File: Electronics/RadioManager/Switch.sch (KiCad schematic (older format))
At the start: 17 parts, among them U1 KSZ8995FQI

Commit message: Annotate existing components
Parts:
- gave numbers to parts that had none: 16
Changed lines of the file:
@@
 Connection ~ 5000 3300
 $Comp
-L +1.8V #PWR?
+L +1.8V #PWR9
 U 1 1 5410F4E8
 P 6200 1700
-F 0 "#PWR?" H 6200 1840 20  0001 C CNN
+F 0 "#PWR9" H 6200 1840 20  0001 C CNN
 F 1 "+1.8V" H 6200 1810 30  0000 C CNN
 F 2 "" H 6200 1700 60  0000 C CNN
@@
 VDDAP
 $Comp
-L C C?
+L C C1
 U 1 1 5410F4F7
 P 6200 2150
-F 0 "C?" H 6250 2300 60  0000 L CNN
+F 0 "C1" H 6250 2300 60  0000 L CNN
 F 1 "C" H 6250 2000 60  0000 L CNN
 F 2 "~" H 6200 2150 60  0000 C CNN
@@
 Connection ~ 6200 1800
 $Comp
-L GND #PWR?
+L GND #PWR10
 U 1 1 5410F557
 P 6200 2500
-F 0 "#PWR?" H 6200 2500 30  0001 C CNN
+F 0 "#PWR10" H 6200 2500 30  0001 C CNN
 F 1 "GND" H 6200 2430 30  0001 C CNN
 F 2 "" H 6200 2500 60  0000 C CNN
@@
 	6200 2500 6200 2400
 $Comp
-L +1.8V #PWR?
+L +1.8V #PWR11
 U 1 1 5410F589
 P 6200 2800
-F 0 "#PWR?" H 6200 2940 20  0001 C CNN
+F 0 "#PWR11" H 6200 2940 20  0001 C CNN
 F 1 "+1.8V" H 6200 2910 30  0000 C CNN
 F 2 "" H 6200 2800 60  0000 C CNN
@@
 VDDAR
 $Comp
-L C C?
+L C C2
 U 1 1 5410F592
 P 6200 3250
-F 0 "C?" H 6250 3400 60  0000 L CNN
+F 0 "C2" H 6250 3400 60  0000 L CNN
 F 1 "C" H 6250 3100 60  0000 L CNN
 F 2 "~" H 6200 3250 60  0000 C CNN
@@
 Connection ~ 6200 2900
 $Comp
-L GND #PWR?
+L GND #PWR12
 U 1 1 5410F59B
 P 6200 3600
-F 0 "#PWR?" H 6200 3600 30  0001 C CNN
+F 0 "#PWR12" H 6200 3600 30  0001 C CNN
 F 1 "GND" H 6200 3530 30  0001 C CNN
 F 2 "" H 6200 3600 60  0000 C CNN
@@
 	6200 3600 6200 3500
 $Comp
-L +3.3V #PWR?
+L +3.3V #PWR24
 U 1 1 5410F5A5
 P 7400 3900
-F 0 "#PWR?" H 7400 3860 30  0001 C CNN
+F 0 "#PWR24" H 7400 3860 30  0001 C CNN
 F 1 "+3.3V" H 7400 4010 30  0000 C CNN
 F 2 "" H 7400 3900 60  0000 C CNN
@@
 VDDAT
 $Comp
-L C C?
+L C C12
 U 1 1 5410F5B4
 P 7400 4350
-F 0 "C?" H 7450 4500 60  0000 L CNN
+F 0 "C12" H 7450 4500 60  0000 L CNN
 F 1 "C" H 7450 4200 60  0000 L CNN
 F 2 "~" H 7400 4350 60  0000 C CNN
@@
 $EndComp
 $Comp
-L GND #PWR?
+L GND #PWR25
 U 1 1 5410F5BA
 P 7400 4700
-F 0 "#PWR?" H 7400 4700 30  0001 C CNN
+F 0 "#PWR25" H 7400 4700 30  0001 C CNN
 F 1 "GND" H 7400 4630 30  0001 C CNN
 F 2 "" H 7400 4700 60  0000 C CNN
@@
 Connection ~ 7400 4000
 $Comp
-L +1.8V #PWR?
+L +1.8V #PWR15
 U 1 1 5410F641
 P 6600 1700
-F 0 "#PWR?" H 6600 1840 20  0001 C CNN
+F 0 "#PWR15" H 6600 1840 20  0001 C CNN
 F 1 "+1.8V" H 6600 1810 30  0000 C CNN
 F 2 "" H 6600 1700 60  0000 C CNN
@@
 VDDC
 $Comp
-L C C?
+L C C4
 U 1 1 5410F64A
 P 6600 2150
-F 0 "C?" H 6650 2300 60  0000 L CNN
+F 0 "C4" H 6650 2300 60  0000 L CNN
 F 1 "C" H 6650 2000 60  0000 L CNN
 F 2 "~" H 6600 2150 60  0000 C CNN
@@
 Connection ~ 6600 1800
 $Comp
-L GND #PWR?
+L GND #PWR16
 U 1 1 5410F653
 P 6600 2500
-F 0 "#PWR?" H 6600 2500 30  0001 C CNN
+F 0 "#PWR16" H 6600 2500 30  0001 C CNN
 F 1 "GND" H 6600 2430 30  0001 C CNN
 F 2 "" H 6600 2500 60  0000 C CNN
@@
 	6600 2500 6600 2400
 $Comp
-L +3.3V #PWR?
+L +3.3V #PWR13
 U 1 1 5410F65B
 P 6200 3900
-F 0 "#PWR?" H 6200 3860 30  0001 C CNN
+F 0 "#PWR13" H 6200 3860 30  0001 C CNN
 F 1 "+3.3V" H 6200 4010 30  0000 C CNN
 F 2 "" H 6200 3900 60  0000 C CNN
@@
 VDDIO
 $Comp
-L C C?
+L C C3
 U 1 1 5410F664
 P 6200 4350
-F 0 "C?" H 6250 4500 60  0000 L CNN
+F 0 "C3" H 6250 4500 60  0000 L CNN
 F 1 "C" H 6250 4200 60  0000 L CNN
 F 2 "~" H 6200 4350 60  0000 C CNN
@@
 $EndComp
 $Comp
-L GND #PWR?
+L GND #PWR14
 U 1 1 5410F66A
 P 6200 4700
-F 0 "#PWR?" H 6200 4700 30  0001 C CNN
+F 0 "#PWR14" H 6200 4700 30  0001 C CNN
 F 1 "GND" H 6200 4630 30  0001 C CNN
 F 2 "" H 6200 4700 60  0000 C CNN
@@
 Connection ~ 6200 4000
 $Comp
-L C C?
+L C C7
 U 1 1 5410F677
 P 7000 2150
-F 0 "C?" H 7050 2300 60  0000 L CNN
+F 0 "C7" H 7050 2300 60  0000 L CNN
 F 1 "C" H 7050 2000 60  0000 L CNN
 F 2 "~" H 7000 2150 60  0000 C CNN
@@
 $EndComp
 $Comp
-L C C?
+L C C10
 U 1 1 5410F67F
 P 7400 2150
-F 0 "C?" H 7450 2300 60  0000 L CNN
+F 0 "C10" H 7450 2300 60  0000 L CNN
 F 1 "C" H 7450 2000 60  0000 L CNN
 F 2 "~" H 7400 2150 60  0000 C CNN
@@
 Connection ~ 7000 1800
 $Comp
-L GND #PWR?
+L GND #PWR19
 U 1 1 5410F6F2
 P 7000 2500
-F 0 "#PWR?" H 7000 2500 30  0001 C CNN
+F 0 "#PWR19" H 7000 2500 30  0001 C CNN
 F 1 "GND" H 7000 2430 30  0001 C CNN
 F 2 "" H 7000 2500 60  0000 C CNN
@@
 $EndComp
 $Comp
-L GND #PWR?
+L GND #PWR22
 U 1 1 5410F6F8
 P 7400 2500
-F 0 "#PWR?" H 7400 2500 30  0001 C CNN
+F 0 "#PWR22" H 7400 2500 30  0001 C CNN
 F 1 "GND" H 7400 2430 30  0001 C CNN
 F 2 "" H 7400 2500 60  0000 C CNN
@@
 	7000 2400 7000 2500
 $Comp
-L C C?
+L C C5
 U 1 1 5410F773
 P 6600 3250
-F 0 "C?" H 6650 3400 60  0000 L CNN
+F 0 "C5" H 6650 3400 60  0000 L CNN
 F 1 "C" H 6650 3100 60  0000 L CNN
 F 2 "~" H 6600 3250 60  0000 C CNN
@@
 $EndComp
 $Comp
-L C C?
+L C C8
 U 1 1 5410F77B
 P 7000 3250
-F 0 "C?" H 7050 3400 60  0000 L CNN
+F 0 "C8" H 7050 3400 60  0000 L CNN
 F 1 "C" H 7050 3100 60  0000 L CNN
 F 2 "~" H 7000 3250 60  0000 C CNN
@@
 $EndComp
 $Comp
-L C C?
+L C C11
 U 1 1 5410F783
 P 7400 3250
-F 0 "C?" H 7450 3400 60  0000 L CNN
+F 0 "C11" H 7450 3400 60  0000 L CNN
 F 1 "C" H 7450 3100 60  0000 L CNN
 F 2 "~" H 7400 3250 60  0000 C CNN
@@
 $EndComp
 $Comp
-L C C?
+L C C13
 U 1 1 5410F78B
 P 7800 3250
-F 0 "C?" H 7850 3400 60  0000 L CNN
+F 0 "C13" H 7850 3400 60  0000 L CNN
 F 1 "C" H 7850 3100 60  0000 L CNN
 F 2 "~" H 7800 3250 60  0000 C CNN
@@
 $EndComp
 $Comp
-L C C?
+L C C15
 U 1 1 5410F793
 P 8200 3250
-F 0 "C?" H 8250 3400 60  0000 L CNN
+F 0 "C15" H 8250 3400 60  0000 L CNN
 F 1 "C" H 8250 3100 60  0000 L CNN
 F 2 "~" H 8200 3250 60  0000 C CNN
@@
 Connection ~ 6600 2900
 $Comp
-L GND #PWR?
+L GND #PWR17
 U 1 1 5410F90F
 P 6600 3600
-F 0 "#PWR?" H 6600 3600 30  0001 C CNN
+F 0 "#PWR17" H 6600 3600 30  0001 C CNN
 F 1 "GND" H 6600 3530 30  0001 C CNN
 F 2 "" H 6600 3600 60  0000 C CNN
@@
 $EndComp
 $Comp
-L GND #PWR?
+L GND #PWR20
 U 1 1 5410F91E
 P 7000 3600
-F 0 "#PWR?" H 7000 3600 30  0001 C CNN
+F 0 "#PWR20" H 7000 3600 30  0001 C CNN
 F 1 "GND" H 7000 3530 30  0001 C CNN
 F 2 "" H 7000 3600 60  0000 C CNN
@@
 $EndComp
 $Comp
-L GND #PWR?
+L GND #PWR23
 U 1 1 5410F92D
 P 7400 3600
-F 0 "#PWR?" H 7400 3600 30  0001 C CNN
+F 0 "#PWR23" H 7400 3600 30  0001 C CNN
 F 1 "GND" H 7400 3530 30  0001 C CNN
 F 2 "" H 7400 3600 60  0000 C CNN
@@
 $EndComp
 $Comp
-L GND #PWR?
+L GND #PWR26
 U 1 1 5410F93C
 P 7800 3600
-F 0 "#PWR?" H 7800 3600 30  0001 C CNN
+F 0 "#PWR26" H 7800 3600 30  0001 C CNN
 F 1 "GND" H 7800 3530 30  0001 C CNN
 F 2 "" H 7800 3600 60  0000 C CNN
@@
 $EndComp
 $Comp
-L GND #PWR?
+L GND #PWR28
 U 1 1 5410F95A
 P 8200 3600
-F 0 "#PWR?" H 8200 3600 30  0001 C CNN
+F 0 "#PWR28" H 8200 3600 30  0001 C CNN
 F 1 "GND" H 8200 3530 30  0001 C CNN
 F 2 "" H 8200 3600 60  0000 C CNN
@@
 	6600 3500 6600 3600
 $Comp
-L C C?
+L C C6
 U 1 1 5410FAC7
 P 6600 4350
-F 0 "C?" H 6650 4500 60  0000 L CNN
+F 0 "C6" H 6650 4500 60  0000 L CNN
 F 1 "C" H 6650 4200 60  0000 L CNN
 F 2 "~" H 6600 4350 60  0000 C CNN
@@
 $EndComp
 $Comp
-L C C?
+L C C9
 U 1 1 5410FACF
 P 7000 4350
-F 0 "C?" H 7050 4500 60  0000 L CNN
+F 0 "C9" H 7050 4500 60  0000 L CNN
 F 1 "C" H 7050 4200 60  0000 L CNN
 F 2 "~" H 7000 4350 60  0000 C CNN
@@
 Connection ~ 6600 4000
 $Comp
-L C C?
+L C C14
 U 1 1 5410FB6A
 P 7800 4350
-F 0 "C?" H 7850 4500 60  0000 L CNN
+F 0 "C14" H 7850 4500 60  0000 L CNN
 F 1 "C" H 7850 4200 60  0000 L CNN
 F 2 "~" H 7800 4350 60  0000 C CNN
@@
 $EndComp
 $Comp
-L C C?
+L C C16
 U 1 1 5410FB72
 P 8200 4350
-F 0 "C?" H 8250 4500 60  0000 L CNN
+F 0 "C16" H 8250 4500 60  0000 L CNN
 F 1 "C" H 8250 4200 60  0000 L CNN
 F 2 "~" H 8200 4350 60  0000 C CNN
@@
 Connection ~ 7800 4000
 $Comp
-L GND #PWR?
+L GND #PWR29
 U 1 1 5410FC13
 P 8200 4700
-F 0 "#PWR?" H 8200 4700 30  0001 C CNN
+F 0 "#PWR29" H 8200 4700 30  0001 C CNN
 F 1 "GND" H 8200 4630 30  0001 C CNN
 F 2 "" H 8200 4700 60  0000 C CNN
@@
 $EndComp
 $Comp
-L GND #PWR?
+L GND #PWR27
 U 1 1 5410FC22
 P 7800 4700
-F 0 "#PWR?" H 7800 4700 30  0001 C CNN
+F 0 "#PWR27" H 7800 4700 30  0001 C CNN
 F 1 "GND" H 7800 4630 30  0001 C CNN
 F 2 "" H 7800 4700 60  0000 C CNN
@@
 $EndComp
 $Comp
-L GND #PWR?
+L GND #PWR21
 U 1 1 5410FC31
 P 7000 4700
-F 0 "#PWR?" H 7000 4700 30  0001 C CNN
+F 0 "#PWR21" H 7000 4700 30  0001 C CNN
 F 1 "GND" H 7000 4630 30  0001 C CNN
 F 2 "" H 7000 4700 60  0000 C CNN
@@
 $EndComp
 $Comp
-L GND #PWR?
+L GND #PWR18
 U 1 1 5410FC40
 P 6600 4700
-F 0 "#PWR?" H 6600 4700 30  0001 C CNN
+F 0 "#PWR18" H 6600 4700 30  0001 C CNN
 F 1 "GND" H 6600 4630 30  0001 C CNN
 F 2 "" H 6600 4700 60  0000 C CNN
@@
 	4900 5600 5000 5600
 $Comp
-L GND #PWR?
+L GND #PWR8
 U 1 1 5410FEC6
 P 5000 5700
-F 0 "#PWR?" H 5000 5700 30  0001 C CNN
+F 0 "#PWR8" H 5000 5700 30  0001 C CNN
 F 1 "GND" H 5000 5630 30  0001 C CNN
 F 2 "" H 5000 5700 60  0000 C CNN
@@
 TXM5
 $Comp
-L GND #PWR?
+L GND #PWR6
 U 1 1 5410FF2C
 P 2000 5400
-F 0 "#PWR?" H 2000 5400 30  0001 C CNN
+F 0 "#PWR6" H 2000 5400 30  0001 C CNN
 F 1 "GND" H 2000 5330 30  0001 C CNN
 F 2 "" H 2000 5400 60  0000 C CNN
@@
 $EndComp
 $Comp
-L GND #PWR?
+L GND #PWR7
 U 1 1 5410FF3B
 P 2000 6500
-F 0 "#PWR?" H 2000 6500 30  0001 C CNN
+F 0 "#PWR7" H 2000 6500 30  0001 C CNN
 F 1 "GND" H 2000 6430 30  0001 C CNN
 F 2 "" H 2000 6500 60  0000 C CNN

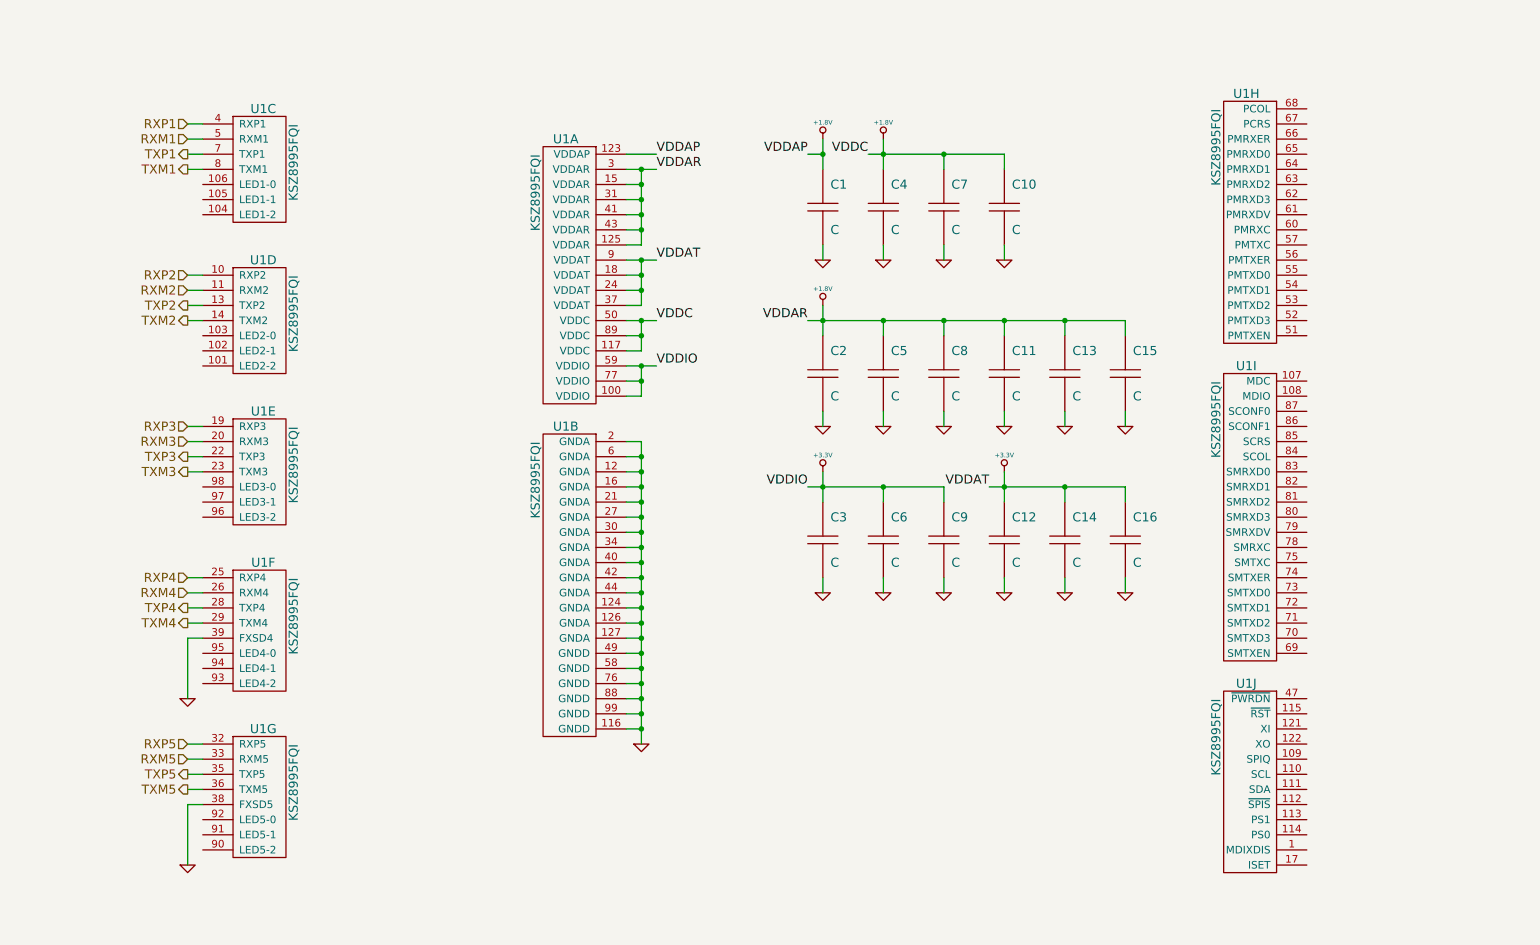
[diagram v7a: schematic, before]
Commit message: Switch support circuitry
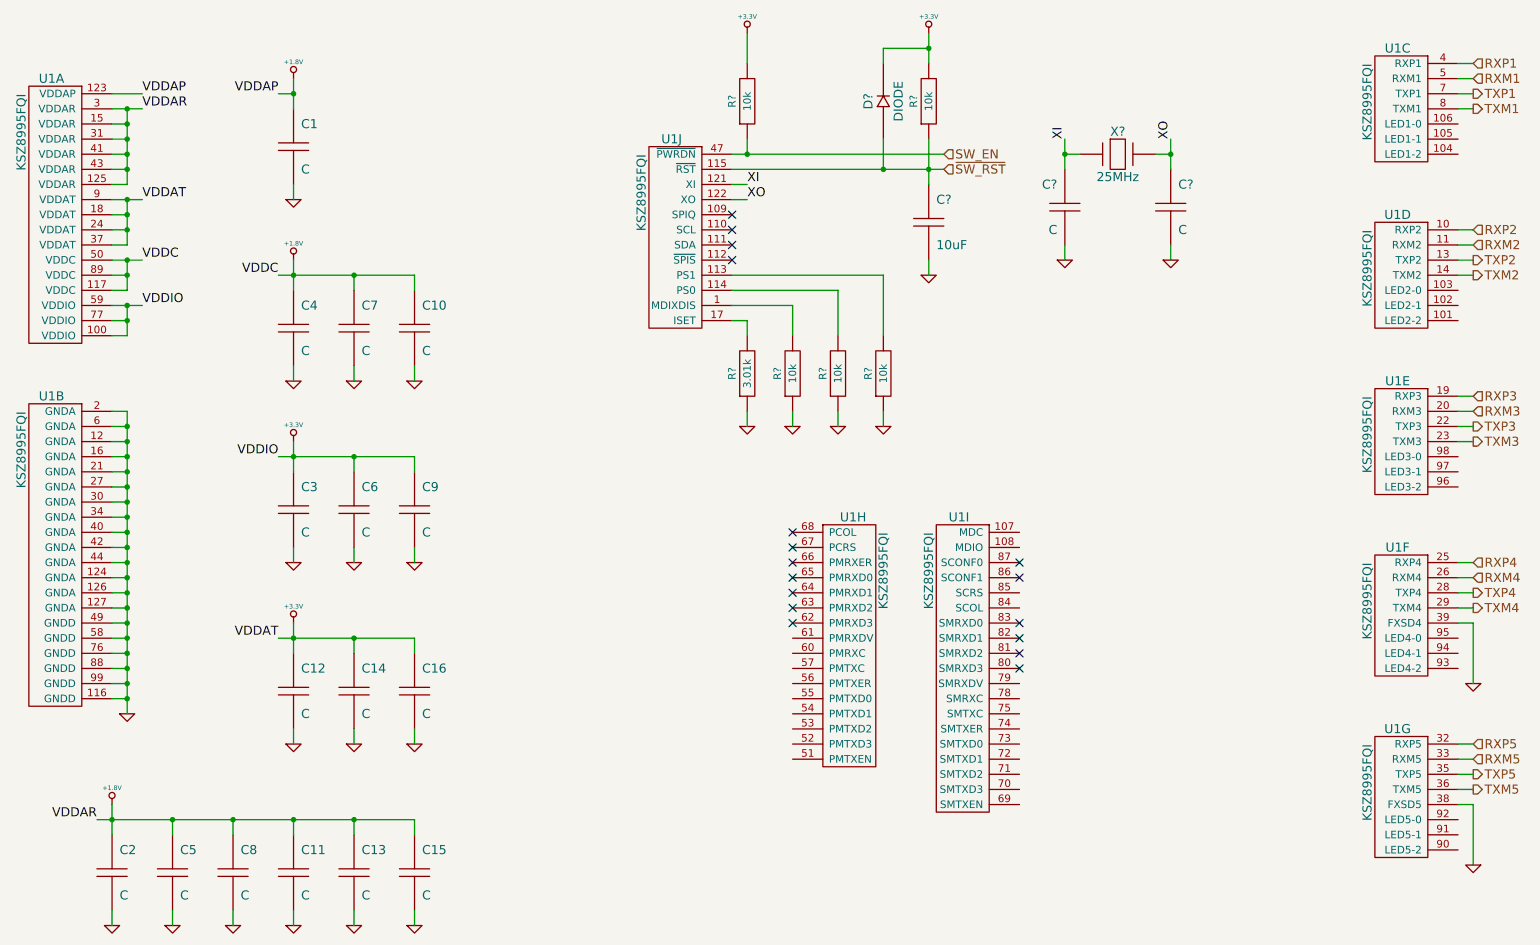
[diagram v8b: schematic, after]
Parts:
- added C?: 10uF, ~, symbol C
- added C? (x2): C, ~, symbol C
- added D?: DIODE, ~, symbol DIODE
- added R?: 3.01k, ~, symbol R
- added R? (x5): 10k, ~, symbol R
- added X?: 25MHz, ~, symbol CRYSTAL
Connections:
- net +3.3V: now also D?.2, R?.2, R?.2
- net GND: now also C?.2, C?.2, C?.2, R?.1, R?.1, R?.1, R?.1
- net at U1.1 (MDIXDIS): now also R?.2
- net at U1.113 (PS1): now also R?.2
- net at U1.114 (PS0): now also R?.2
- net ~SW_RST: now reaches U1.115 (~RST)
- net ~SW_RST: now also C?.1, D?.1, R?.1
- net XI: now reaches U1.121 (XI)
- net XI: now also C?.1, X?.1
- net XO: now reaches U1.122 (XO)
- net XO: now also C?.1, X?.2
- net at U1.17 (ISET): now also R?.2
- net SW_EN: now reaches U1.47 (~PWRDN)
- net SW_EN: now also R?.1
- no-connect marks 0 -> 17
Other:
- moved on the sheet: C1, C10, C11, C12, C13, C14, C15, C16, C2, C3, C4, C5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
